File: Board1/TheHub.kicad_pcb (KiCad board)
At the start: 2 copper layers, 118.7 x 184.1 mm, 51 parts, among them J11 RFD900, J12 I2C_1 Test Point, J13 I2C_2 Test Point, J15 GPIO Test, J16 I2C_3 Test Point, J17 12V OUT, J23 NucleoRight, J5 NucleoLeft, J8 12V MAIN POWER, U10 ADXL377, U11 BNO055, U12 MPL115A2, U13 GPS, U6 TL1963, U7 LM340MP-5.0, U8 MCP9808

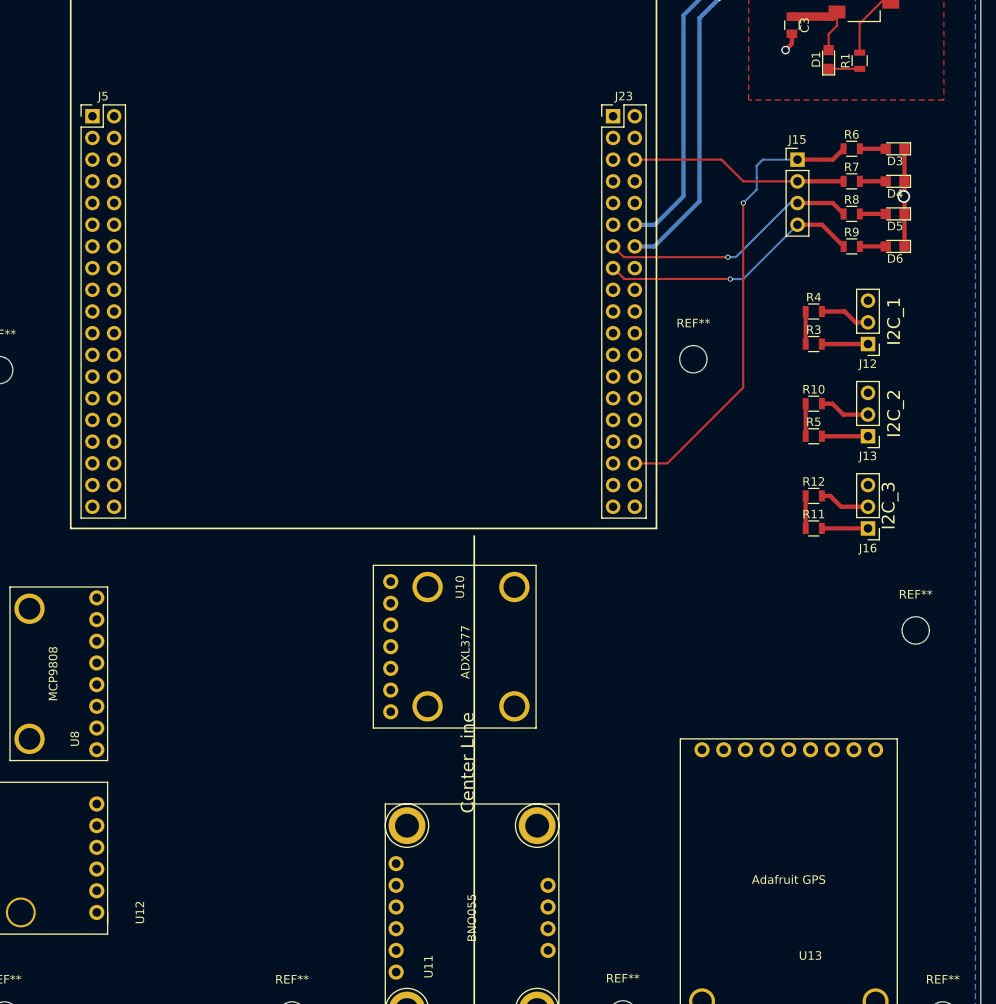
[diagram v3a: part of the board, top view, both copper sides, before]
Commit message: Route all signal and power traces
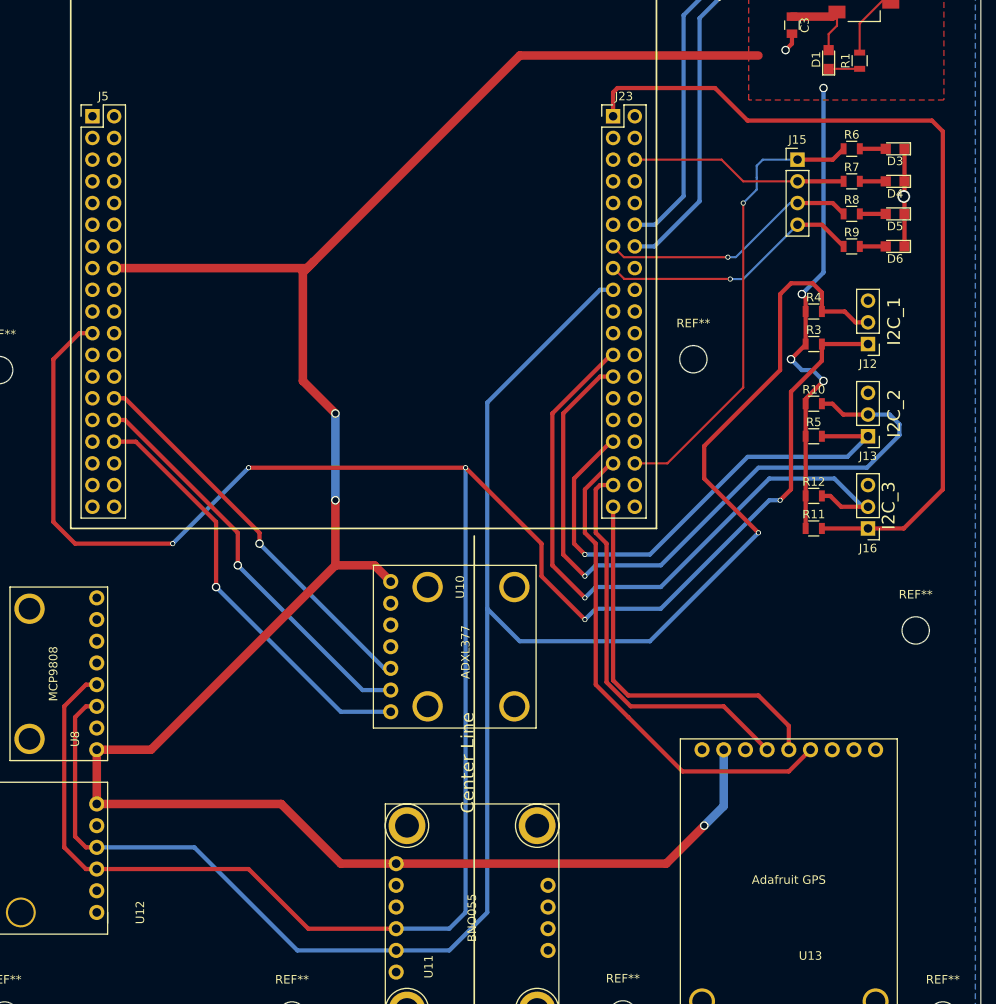
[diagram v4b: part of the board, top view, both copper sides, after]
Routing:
- net +3V3: track 21.8 -> 326.7 mm, vias 0 -> 7
- net /PB7: track 5.72 -> 281.3 mm, vias 0 -> 5
- net /PB6: track 5.93 -> 239.4 mm, vias 0 -> 1
- net /PC9: track 5.40 -> 101.7 mm
- net /PB10: track 5.93 -> 82.8 mm, vias 0 -> 1
- net /PA8: track 5.93 -> 79.3 mm, vias 0 -> 1
- net /GPS_FIX: track 0.00 -> 58.4 mm
- net /PB3: track 5.40 -> 60.1 mm, vias 0 -> 1
- net /A2: track 0.00 -> 49.9 mm, vias 0 -> 1
- net /A1: track 0.00 -> 47.7 mm, vias 0 -> 1
- net /PA2: track 0.00 -> 47.4 mm
- net /A0: track 0.00 -> 46.2 mm, vias 0 -> 1
- net /PA3: track 0.00 -> 45.9 mm
